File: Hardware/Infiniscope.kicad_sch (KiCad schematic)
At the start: 11 parts, among them J1 USB_C_Receptacle_USB2.0_16P, SW1 SW_Push, U1 RP2350A, U2 MCP1700x-330xxTT, U3 W25Q128JVP, Y1 Crystal_GND24

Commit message: new Schematic
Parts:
- added C10, C11, C12, C13, C3, C4, C5, C6, C7, C8, C9: 100n, symbol Device:C
- added J2: Conn_Coaxial, symbol Connector:Conn_Coaxial
- added L1: 3.3u, symbol Device:L
- added U4: AD9238BSTRL-65, ad9238:ST_64_1_ADI, symbol ed2e:AD9238BSTRL-65
- added U5: OPA2320AIDGKR, ad9238:DGK8, symbol ed2e:OPA2320AIDGKR
- added U6: REF5025ID, ad9238:D8, symbol ed2e:REF5025ID
- added U7: TLV3502AIDR, ad9238:D8, symbol ed2e:TLV3502AIDR
- added U9: PGA281AxPW, Package_SO:TSSOP-16_4.4x5mm_P0.65mm, symbol Analog:PGA281AxPW
- added Y2: 10 mhz cmos oscillator, Oscillator:Oscillator_SMD_Abracon_ASE-4Pin_3.2x2.5mm, symbol Oscillator:ASE-xxxMHz
- SW1: footprint (none) -> Button_Switch_SMD:SW_SPST_PTS810
- Y1: footprint (none) -> Crystal:Crystal_SMD_0603-4Pin_6.0x3.5mm
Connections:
- net +1V1: now also C10.1, C11.1, C12.1
- net +3V3: now also U1.44 (ADC_AVDD), U1.46 (VREG_AVDD), U1.49 (VREG_VIN), U1.53 (USB_OTP_VDD), U1.54 (QSPI_IOVDD), C13.1, C3.1, C4.1, C5.1, C6.1, C7.1, C8.1, C9.1, U4.12 (AVDD), U4.17 (AVDD), U4.19 (DCS), U4.29 (DRVDD), U4.41 (DRVDD), U4.5 (AVDD), U4.52 (DRVDD), U4.64 (AVDD), U6.2 (VIN), U7.8 (V+), Y2.1 (EN), Y2.4 (Vdd)
- net GND: now also C10.2, C11.2, C12.2, C13.2, C3.2, C4.2, C5.2, C6.2, C7.2, C8.2, C9.2, J2.2 (Ext), U4.1 (AGND), U4.13 (AGND), U4.16 (AGND), U4.20 (DFS), U4.28 (DRGND), U4.4 (AGND), U4.40 (DRGND), U4.53 (DRGND), U4.59 (OEB_A), U4.60 (PDWN_A), U5.4 (V-), U6.4 (GND), U7.5 (V-), Y2.2 (GND)
- net GP7: now reaches U1.10 (GPIO7)
- net GP7: now also U4.50 (D6_A)
- net GP8: now reaches U1.12 (GPIO8)
- net GP8: now also U4.51 (D7_A)
- net GP9: now reaches U1.13 (GPIO9)
- net GP9: now also U4.54 (D8_A)
- net GP10: now reaches U1.14 (GPIO10)
- net GP10: now also U4.55 (D9_A)
- net GP11: now reaches U1.15 (GPIO11)
- net GP11: now also U4.56 (D10_A)
- net GP12: now reaches U1.16 (GPIO12)
- net GP12: now also U7.7 (OUTA)
- net GP13: now reaches U1.17 (GPIO13)
- net GP1: now reaches U1.3 (GPIO1)
- net GP1: now also U4.44 (D0_A)
- net GP2: now reaches U1.4 (GPIO2)
- net GP2: now also U4.45 (D1_A)
- net at U1.48 (VREG_LX): now also L1.2
- net GP3: now reaches U1.5 (GPIO3)
- net GP3: now also U4.46 (D2_A)
- net GP4: now reaches U1.7 (GPIO4)
- net GP4: now also U4.47 (D3_A)
- net GP5: now reaches U1.8 (GPIO5)
- net GP5: now also U4.48 (D4_A)
- net GP6: now reaches U1.9 (GPIO6)
- net GP6: now also U4.49 (D5_A)
- new net ADC_CLK: U4.18 (CLK_B), U4.63 (CLK_A), Y2.3 (OUT)
- new net ADC_VREF: U4.8 (VREF), U6.6 (VOUT)
- new net IN1+: J2.1 (In), U5.3 (INA+), U7.1 (INA+)
- new net OUTA: U4.2 (VIN+_A), U5.1 (OUTA)
- no-connect marks 4 -> 12

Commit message: Updated PCB layout
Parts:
- removed U9: PGA281AxPW, Package_SO:TSSOP-16_4.4x5mm_P0.65mm, symbol Analog:PGA281AxPW
- added J4: 5051101297, ad9238:CON_5051101297_MOL, symbol ed2e:5051101297
- C1, C10, C11, C12, C13, C2, C3, C4, C5, C6, C7, C8, C9: footprint (none) -> Capacitor_SMD:C_0402_1005Metric
- J1: footprint (none) -> Connector_USB:USB_C_Receptacle_HCTL_HC-TYPE-C-16P-01A
- J2: footprint (none) -> Connector_Coaxial:BNC_TEConnectivity_1478035_Horizontal
- L1: footprint (none) -> Inductor_SMD:L_0805_2012Metric
- R1, R2, R3: footprint (none) -> Resistor_SMD:R_0402_1005Metric
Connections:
- net +1V1: now also L1.2, U1.50 (VREG_FB)
- net +3V3: now also U3.8 (VCC), U5.8 (V+), J4.3, J4.4
- net GND: now also J4.1, J4.12, J4.2, J4.5, J4.6, J4.P1, J4.P2
- net GP1: now also U4.56 (D10_A); no longer U4.44 (D0_A)
- net GP10: now also U4.45 (D1_A); no longer U4.55 (D9_A)
- net GP11: now also U4.44 (D0_A); no longer U4.56 (D10_A)
- net GP2: now also U4.55 (D9_A); no longer U4.45 (D1_A)
- net GP3: now also U4.54 (D8_A); no longer U4.46 (D2_A)
- net GP4: now also U4.51 (D7_A); no longer U4.47 (D3_A)
- net GP5: now also U4.50 (D6_A); no longer U4.48 (D4_A)
- net GP7: now also U4.48 (D4_A); no longer U4.50 (D6_A)
- net GP8: now also U4.47 (D3_A); no longer U4.51 (D7_A)
- net GP9: now also U4.46 (D2_A); no longer U4.54 (D8_A)
- net CS: now reaches U1.18 (GPIO14)
- net CS: now also J4.8
- net SCL: now reaches U1.19 (GPIO15)
- net SCL: now also J4.9
- net SDA: now reaches U1.27 (GPIO16)
- net SDA: now also J4.10
- net RESET: now reaches U1.28 (GPIO17)
- net RESET: now also J4.11
- net at U1.48 (VREG_LX): now also L1.1; no longer L1.2
- net GP13 renamed D/C
- net D/C: now also J4.7
- no-connect marks 12 -> 61
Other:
- note added: "ADC"
- moved on the sheet: L1

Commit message: updated pcb
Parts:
- removed C13: 100n, Capacitor_SMD:C_0402_1005Metric, symbol Device:C
- added C14: 100n, Capacitor_SMD:C_0402_1005Metric, symbol Device:C
- added R4, R5, R6, R7, R8, R9: 10K, Resistor_SMD:R_0402_1005Metric, symbol Device:R
- added SW2, SW3, SW4, SW5, SW6, SW7: SW_Push, Button_Switch_SMD:SW_SPST_PTS810, symbol Switch:SW_Push
- Y1: footprint Crystal:Crystal_SMD_0603-4Pin_6.0x3.5mm -> Crystal:Crystal_SMD_3225-4Pin_3.2x2.5mm
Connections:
- net +3V3: now also C14.1, R4.1, R5.1, R6.1, R7.1, R8.1, R9.1
- net GND: now also C14.2, SW2.1, SW3.1, SW4.1, SW5.1, SW6.1, SW7.1
- net BTN_BACK: now reaches U1.29 (GPIO18)
- net BTN_BACK: now also R5.2, SW3.2
- net BTN_DOWN: now reaches U1.31 (GPIO19)
- net BTN_DOWN: now also R8.2, SW7.2
- net BTN_MENU: now reaches U1.32 (GPIO20)
- net BTN_MENU: now also R6.2, SW4.2
- net BTN_UP: now reaches U1.33 (GPIO21)
- net BTN_UP: now also R9.2, SW6.2
- net BTN_RUN: now reaches U1.34 (GPIO22)
- net BTN_RUN: now also R7.2, SW5.2
- net BTN_PWR: now reaches U1.35 (GPIO23)
- net BTN_PWR: now also R4.2, SW2.2
- no-connect marks 61 -> 55

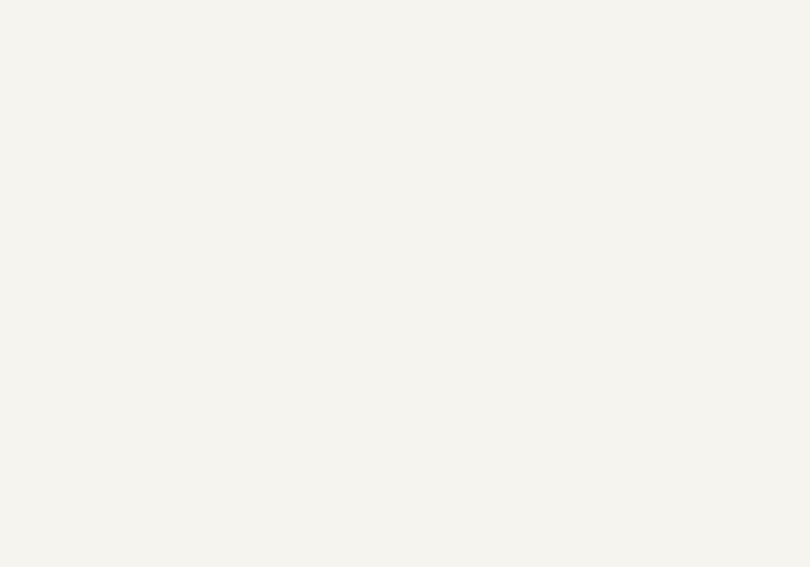
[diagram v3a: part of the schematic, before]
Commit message: added mounting holes
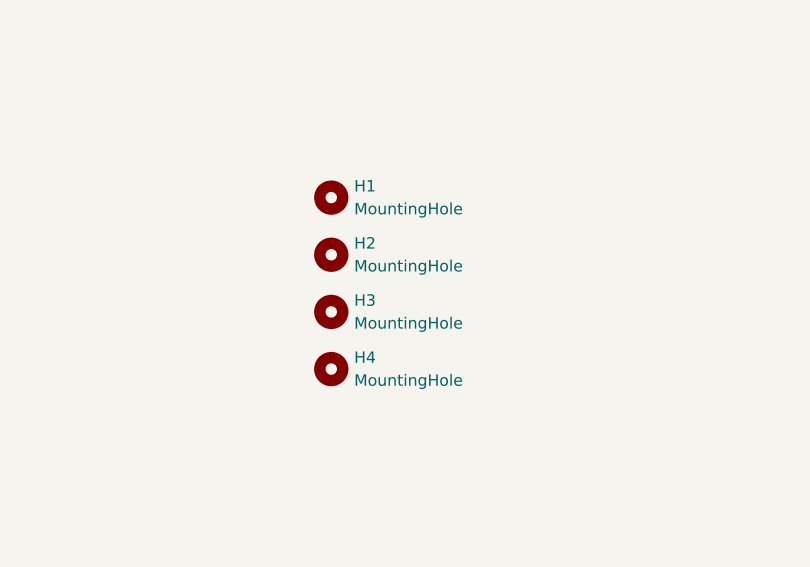
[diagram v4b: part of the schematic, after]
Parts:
- added H1, H2, H3, H4: MountingHole, MountingHole:MountingHole_3.2mm_M3, symbol Mechanical:MountingHole

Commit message: added 3d files
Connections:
- net GND: now also U7.2 (INA-)
- no-connect marks 55 -> 54
